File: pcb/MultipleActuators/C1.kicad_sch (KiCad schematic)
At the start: 26 parts, among them J1 Screw_Terminal_01x02, J12 Screw_Terminal_01x03, J2 Screw_Terminal_01x02, J3 Screw_Terminal_01x02, J4 Screw_Terminal_01x02, J5 Screw_Terminal_01x02, J6 Screw_Terminal_01x02, J7 Screw_Terminal_01x02, Q1 BT136-500, Q2 BT136-500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

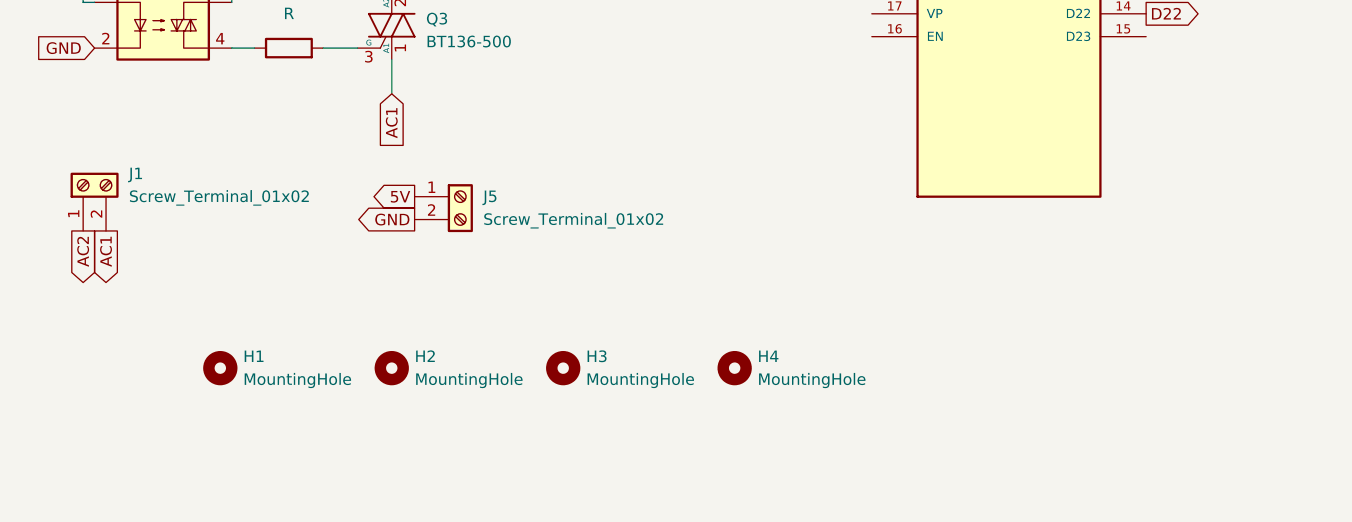
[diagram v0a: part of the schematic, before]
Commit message: Update
now this adds the HLK-PM01 so that this can have it's own AC-DC adapter built in, and has way more comfortable connection cable management inside a box. Next iterations will be replacing the connectors for the SDA and SCL (and all those 7 signal pins) for more robust and compact ones. In this iteration the sizing of the AC traces were all changed to match a 3mm width which allows for 5A input current handling at most, with a delta of 10°C.
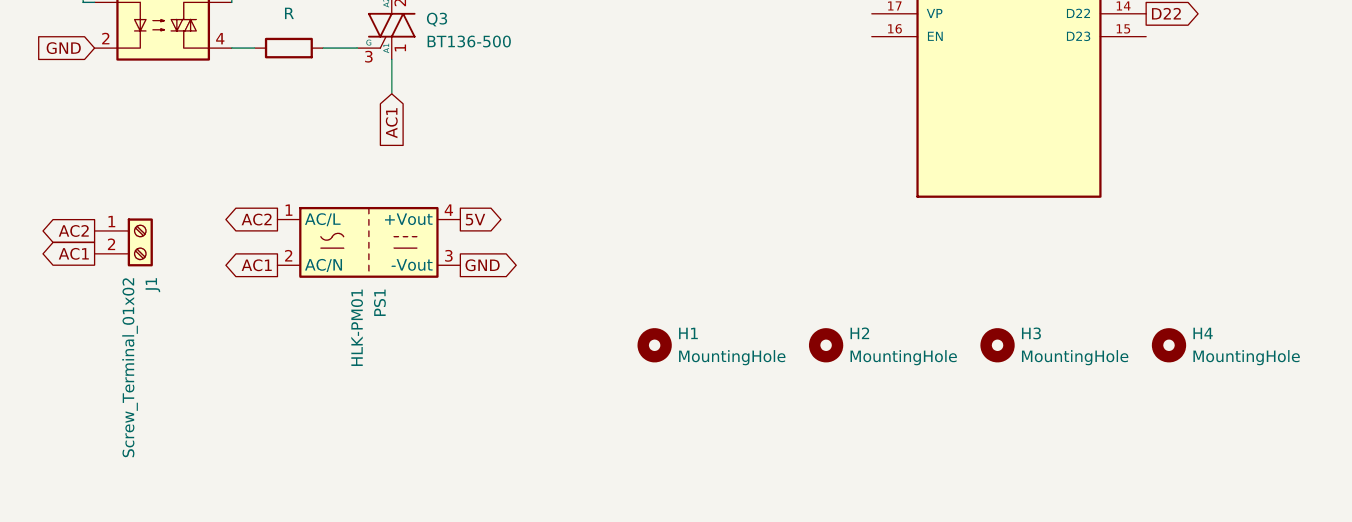
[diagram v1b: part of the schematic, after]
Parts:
- removed J5: Screw_Terminal_01x02, TerminalBlock:TerminalBlock_Altech_AK300-2_P5.00mm, symbol Connector:Screw_Terminal_01x02
- added PS1: HLK-PM01, Converter_ACDC:Converter_ACDC_Hi-Link_HLK-PMxx, symbol Converter_ACDC:HLK-PM01
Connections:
- net 5V: now also PS1.4 (+Vout)
- net AC1: now also PS1.2 (AC/N)
- net AC2: now also PS1.1 (AC/L)
- net GND: now also PS1.3 (-Vout)
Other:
- moved on the sheet: H1, H2, H3, H4, J1
